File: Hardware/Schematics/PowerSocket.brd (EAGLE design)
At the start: 100 x 47.5 mm, 74 parts, among them T1 BT138-V, T2 BT138-V, T3 BT138-V, T4 BT138-V, T5 BT138-V, T6 BT138-V

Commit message: New board layout
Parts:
- removed ACIN-NULL, ACIN-PHASE, ACOUT-NULL, ACOUT-NULL1, ACOUT-NULL2, ACOUT-PHASE, ACOUT-PHASE1, ACOUT-PHASE2: -, wirepad:3,81/1,4
- removed BUTTON_LED+: BUTTON_VCC, wirepad:2,15/1,0
- removed BUTTON_LED+1, BUTTON_LED+2, BUTTON_LED-, BUTTON_LED-1, BUTTON_LED-2, BUTTON_SWITCH1, BUTTON_SWITCH3, BUTTON_SWITCH5: -, wirepad:2,15/1,0
- removed U$1, U$3, U$4: ACS710, PowerSocket:SO-16DW
- added AMP1, AMP2, AMP3: ACS710, PowerSocket:SO-16DW
- added BUTTON1_VCC: (no value), wirepad:2,15/1,0
- added BUTTON2_VCC, BUTTON3_VCC, LED1, LED2, LED3, SWITCH1, SWITCH2, SWITCH3: -, wirepad:2,15/1,0
- added NULL, NULL1-OUT, NULL2-OUT, NULL3-OUT, PHASE, PHASE1-OUT, PHASE2-OUT, PHASE3-OUT: -, wirepad:3,81/1,4
- added R24: 0, eagle-ltspice:R2010
- R14, R18: device rcl:C0805 -> rcl:R0805
- T1, T2, T3, T4, T5, T6: value BT138-V -> BT138-H; device triac:TO220BV -> triac:TO220BH
- moved R9 83.6 mm to (89.3, 19.7), turned to 270 degrees
- moved R10 79.9 mm to (80.9, 30.8), turned to 180 degrees
- moved C11 71.6 mm to (85.7, 27.1)
- moved R3 69.1 mm to (83.4, 26.1)
- moved C10 67.3 mm to (85.5, 20.0), flipped to the bottom
- moved R4 66.1 mm to (79.3, 19.3), turned to 0 degrees
- moved C9 65.5 mm to (81.1, 27.6), flipped to the bottom
- moved T2 56.8 mm to (61.0, 13.5), turned to 0 degrees
- moved R11 56.4 mm to (96.1, 56.7), flipped to the top
- moved R15 55.9 mm to (79.0, 29.2), turned to 180 degrees
- moved R12 55.7 mm to (89.3, 23.1), turned to 270 degrees
- moved OK2 55.3 mm to (61.0, 15.5)
- moved R13 52.5 mm to (77.1, 12.9), turned to 0 degrees
- moved C1 49.3 mm to (86.6, 31.4), flipped to the bottom
- moved C4 49.2 mm to (88.6, 31.4), flipped to the bottom
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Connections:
- net N$25 renamed GATE2
- net N$3 renamed VOLTMETER
- removed net N$15 (its old number): BUTTON_LED-.1, R7.1
- removed net N$2 (its old number): R1.1, RESET.4, U$2.EN
- removed net N$36 (its old number): ACOUT-PHASE1.1, U$3.5, U$3.6, U$3.7, U$3.8
- removed net N$40: U$3.13
- removed net N$42 (its old number): OK5.2, R16.2
- removed net N$43: OK5.6, R17.1
- removed net N$45: ACIN-NULL.1, R5.1, T1.T1, T3.T1, T5.T1
- removed net N$46: OK6.2, R18.1
- removed net N$47: OK6.6, R19.1
- removed net N$49: R19.2, T6.T2, U$4.1, U$4.2, U$4.3, U$4.4
- removed net N$50: U$4.13
- removed net N$51: ACIN-PHASE.1, D1.C, T2.T1, T4.T1, T6.T1
- removed net N$52: R22.2, U$2.IO5
- removed net N$53: R15.2, T4.T2, U$3.1, U$3.2, U$3.3, U$3.4
- removed net N$54: R16.1, R18.2, U$2.IO27
- removed net N$55: C9.2, U$1.11
- removed net N$60: C10.2, U$1.10
- removed net N$62: C1.2, U$3.11
- removed net N$63: C4.2, U$3.10
- removed net N$64: C5.2, U$4.11
- removed net N$65: C6.2, U$4.10
- new net AMP1: AMP1.12, U$2.IO34
- new net AMP2: AMP2.12, U$2.IO35
- new net AMP3: AMP3.12, U$2.IO32
- new net BUTTON1: R8.1, SWITCH1.1, U$2.IO22
- new net BUTTON2: R21.1, SWITCH2.1, U$2.IO23
- new net BUTTON3: R23.1, SWITCH3.1, U$2.IO5
- new net GATE1: R3.2, R9.2, U$2.IO25
- new net GATE3: R16.1, R18.1, U$2.IO27
- new net LED1: R7.2, U$2.IO19
- new net LED2: R20.2, U$2.IO18
- new net LED3: R22.2, U$2.IO17
- new net N$24: FLASH.3, FLASH.4, R2.2, U$2.IO0
- new net N$30: AMP2.10, C4.1
- new net N$66: R1.1, RESET.3, RESET.4, U$2.EN
- new net NULL: NULL.1, R5.1, T2.T1, T4.T1, T6.T1
- new net PHASE: PHASE.1, R24.2, T1.T1, T3.T1, T5.T1
- new net PHASE1: AMP1.1, AMP1.2, AMP1.3, AMP1.4, R10.2, T1.T2
- new net PHASE2: AMP2.1, AMP2.2, AMP2.3, AMP2.4, R15.2, T3.T2
- new net PHASE3: AMP3.1, AMP3.2, AMP3.3, AMP3.4, R19.2, T5.T2
- net GND: now also AMP1.16, AMP1.9, AMP2.16, AMP2.9, AMP3.16, AMP3.9, C1.2, C10.2, C11.2, C12.2, C13.2, C4.2, C5.2, C6.2, C9.2, FLASH.1, R21.2, R23.2, R8.2, RESET.2; no longer C1.1, C10.1, C11.1, C12.1, C13.1, C4.1, C5.1, C6.1, C9.1, R21.1, R23.1, R8.1, U$1.16, U$1.9, U$3.16, U$3.9, U$4.16, U$4.9
- net N$1: now also OK1.2, R9.1; no longer ACOUT-NULL.1, R4.2, T1.T2
- net N$10: now also AMP3.5, AMP3.6, AMP3.7, AMP3.8, PHASE3-OUT.1; no longer OK2.2, R9.1
- net N$11: now also LED3.1, R22.1; no longer U$2.IO35, U$3.12
- net N$12: now also AMP1.10, C10.1; no longer U$1.12, U$2.IO34
- net N$13: now also AMP1.11, C9.1; no longer ACOUT-PHASE.1, U$1.5, U$1.6, U$1.7, U$1.8
- net N$14: now also NULL2-OUT.1, T4.T2; no longer ACOUT-NULL1.1, T3.T2
- net N$16: now also OK4.6, R13.1; no longer BUTTON_LED-1.1, R20.1
- net N$17: now also NULL1-OUT.1, R4.2, T2.T2; no longer BUTTON_SWITCH1.1, R8.2, U$2.IO19
- net N$18: now also OK5.2, R18.2; no longer OK1.6, R4.1
- net N$20: now also OK1.6, R10.1; no longer BUTTON_SWITCH3.1, R21.2, U$2.IO18
- net N$21: now also R4.1; no longer R10.1
- net N$23: now also OK3.6, R15.1; no longer R10.2, T2.T2, U$1.1, U$1.2, U$1.3, U$1.4
- net N$26: now also AMP2.5, AMP2.6, AMP2.7, AMP2.8, PHASE2-OUT.1; no longer BUTTON_LED-2.1, R22.1
- net N$27: now also AMP1.5, AMP1.6, AMP1.7, AMP1.8, PHASE1-OUT.1; no longer U$1.13
- net N$28: now also R14.1; no longer R12.2
- net N$29: now also OK4.2, R12.2; no longer OK3.6, R13.1
- net N$31: now also OK6.2, R16.2; no longer R20.2, U$2.IO23
- net N$32: now also AMP2.11, C1.1; no longer OK4.2, R14.1
- net N$33: now also OK6.6, R17.1; no longer OK4.6, R15.1
- net N$35: now also OK5.6, R19.1; no longer ACOUT-PHASE2.1, U$4.5, U$4.6, U$4.7, U$4.8
- net N$38: now also AMP3.10, C6.1; no longer ACOUT-NULL2.1, R17.2, T5.T2
- net N$39: now also AMP3.11, C5.1; no longer BUTTON_SWITCH5.1, R23.2, U$2.IO17
- net N$41: now also D1.C, R24.1; no longer U$2.IO32, U$4.12
- net N$6: now also OK2.2, R3.1; no longer OK1.2, R3.2
- net N$7: now also LED2.1, R20.1; no longer FLASH.3, R2.2, U$2.IO0
- net N$8: now also NULL3-OUT.1, R17.2, T6.T2; no longer R3.1, R9.2, U$2.IO25
- net N$9: now also LED1.1, R7.1; no longer R7.2, U$2.IO22
- net VCC: now also AMP1.14, AMP1.15, AMP2.14, AMP2.15, AMP3.14, AMP3.15, BUTTON1_VCC.1, BUTTON2_VCC.1, BUTTON3_VCC.1, C11.1, C12.1, C13.1; no longer BUTTON_LED+.1, BUTTON_LED+1.1, BUTTON_LED+2.1, C11.2, C12.2, C13.2, U$1.14, U$1.15, U$3.14, U$3.15, U$4.14, U$4.15
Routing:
- net VCC: track 252.8 -> 0.00 mm, vias 10 -> 0
- net GND: track 181.0 -> 0.00 mm, vias 6 -> 0
- net N$8: track 93.5 -> 0.00 mm, vias 1 -> 0
- net N$12: track 87.8 -> 0.00 mm
- net N$11: track 70.5 -> 0.00 mm
- net N$45: track 59.3 -> 0.00 mm
- net N$51: track 58.8 -> 0.00 mm
- net GATE2: track 55.9 -> 0.00 mm, vias 2 -> 0
- net N$68: track 47.4 -> 0.00 mm
- net N$41: track 41.9 -> 0.00 mm, vias 2 -> 0
- net N$54: track 40.1 -> 0.00 mm, vias 1 -> 0
- net N$7: track 39.8 -> 0.00 mm, vias 3 -> 0
- net N$37: track 34.3 -> 0.00 mm
- net VOLTMETER: track 18.5 -> 0.00 mm, vias 1 -> 0
- net N$17: track 14.2 -> 0.00 mm, vias 1 -> 0
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- removed copper zone on layer 1, net GND
- removed copper zone on layer 16, net GND

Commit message: Added .brd script.
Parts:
- removed BUTTON1_VCC: (no value), wirepad:2,15/1,0
- removed BUTTON2_VCC, BUTTON3_VCC, LED1, LED2, LED3, SWITCH1, SWITCH2, SWITCH3: -, wirepad:2,15/1,0
- removed U$2: ESP3212LABELS, esp3212-ptw:ESP3212
- added BUTTON1, BUTTON2, BUTTON3: (no value), pinhead:1X03
- added ESP3212: ESP3212LABELS, esp3212-ptw:ESP3212
- moved C2 84.5 mm to (5.31, 73.5)
- moved R18 79.3 mm to (6.00, 24.0)
- moved C1 78.4 mm to (14.6, 62.2), flipped to the top, turned to 0 degrees
- moved R17 77.3 mm to (9.00, 10.0)
- moved R19 73.2 mm to (14.0, 41.0)
- moved C11 67.8 mm to (38.7, 75.9), flipped to the top
- moved R16 63.8 mm to (17.0, 23.5)
- moved C6 61.9 mm to (41.9, 67.6), flipped to the top, turned to 0 degrees
- moved C5 61.8 mm to (27.3, 65.8), flipped to the top, turned to 0 degrees
- moved SUPPLY_3.3 59.9 mm to (93.5, 1.96)
- moved C10 57.8 mm to (58.1, 71.0), flipped to the top, turned to 0 degrees
- moved SUPPLY_GND 57.2 mm to (93.5, 4.50)
- moved C4 54.3 mm to (49.4, 68.9), flipped to the top, turned to 0 degrees
- moved R12 50.3 mm to (39.0, 23.5)
- moved C9 49.1 mm to (40.4, 54.9), flipped to the top, turned to 0 degrees
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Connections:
- net AMP1: now also ESP3212.IO34; no longer U$2.IO34
- net AMP2: now also ESP3212.IO35; no longer U$2.IO35
- net AMP3: now also ESP3212.IO32; no longer U$2.IO32
- net BUTTON1: now also BUTTON1.3, ESP3212.IO22; no longer SWITCH1.1, U$2.IO22
- net BUTTON2: now also BUTTON2.3, ESP3212.IO23; no longer SWITCH2.1, U$2.IO23
- net BUTTON3: now also BUTTON3.3, ESP3212.IO5; no longer SWITCH3.1, U$2.IO5
- net GATE1: now also ESP3212.IO25; no longer U$2.IO25
- net GATE2: now also ESP3212.IO26; no longer U$2.IO26
- net GATE3: now also ESP3212.IO27; no longer U$2.IO27
- net GND: now also ESP3212.GND_B, ESP3212.GND_L, ESP3212.GND_R, ESP3212.IO2; no longer U$2.GND_B, U$2.GND_L, U$2.GND_R, U$2.IO2
- net LED1: now also ESP3212.IO19; no longer U$2.IO19
- net LED2: now also ESP3212.IO18; no longer U$2.IO18
- net LED3: now also ESP3212.IO17; no longer U$2.IO17
- net N$11: now also BUTTON3.2; no longer LED3.1
- net N$2: now also ESP3212.IO15; no longer U$2.IO15
- net N$24: now also ESP3212.IO0; no longer U$2.IO0
- net N$3: now also ESP3212.IO13; no longer U$2.IO13
- net N$4: now also ESP3212.IO12; no longer U$2.IO12
- net N$5: now also ESP3212.IO14; no longer U$2.IO14
- net N$66: now also ESP3212.EN; no longer U$2.EN
- net N$7: now also BUTTON2.2; no longer LED2.1
- net N$70: now also ESP3212.U0TX; no longer U$2.U0TX
- net N$77: now also ESP3212.U0RX; no longer U$2.U0RX
- net N$9: now also BUTTON1.2; no longer LED1.1
- net VCC: now also BUTTON1.1, BUTTON2.1, BUTTON3.1, ESP3212.3V3; no longer BUTTON1_VCC.1, BUTTON2_VCC.1, BUTTON3_VCC.1, U$2.3V3
- net VOLTMETER: now also ESP3212.IO4; no longer U$2.IO4
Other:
- board size 100 x 47.5 mm -> 100 x 80 mm

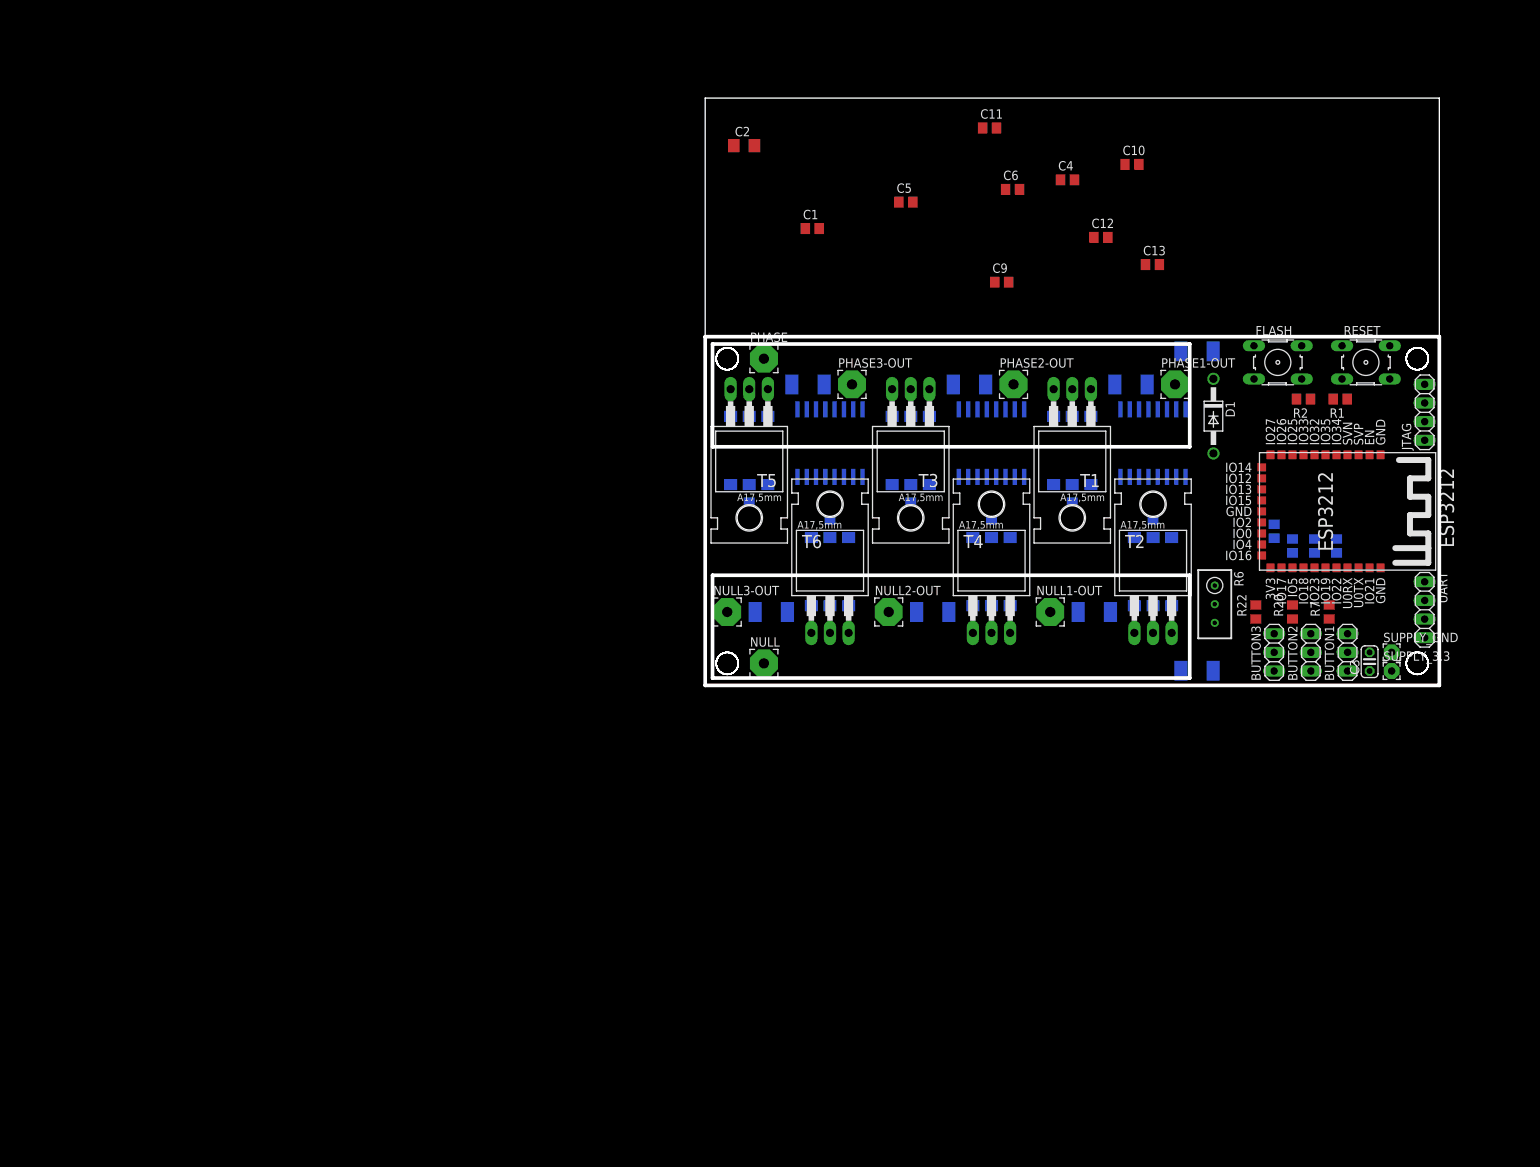
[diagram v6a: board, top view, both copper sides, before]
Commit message: Changed amp-meters and added 5V step-up. I probably don't have the correct package.
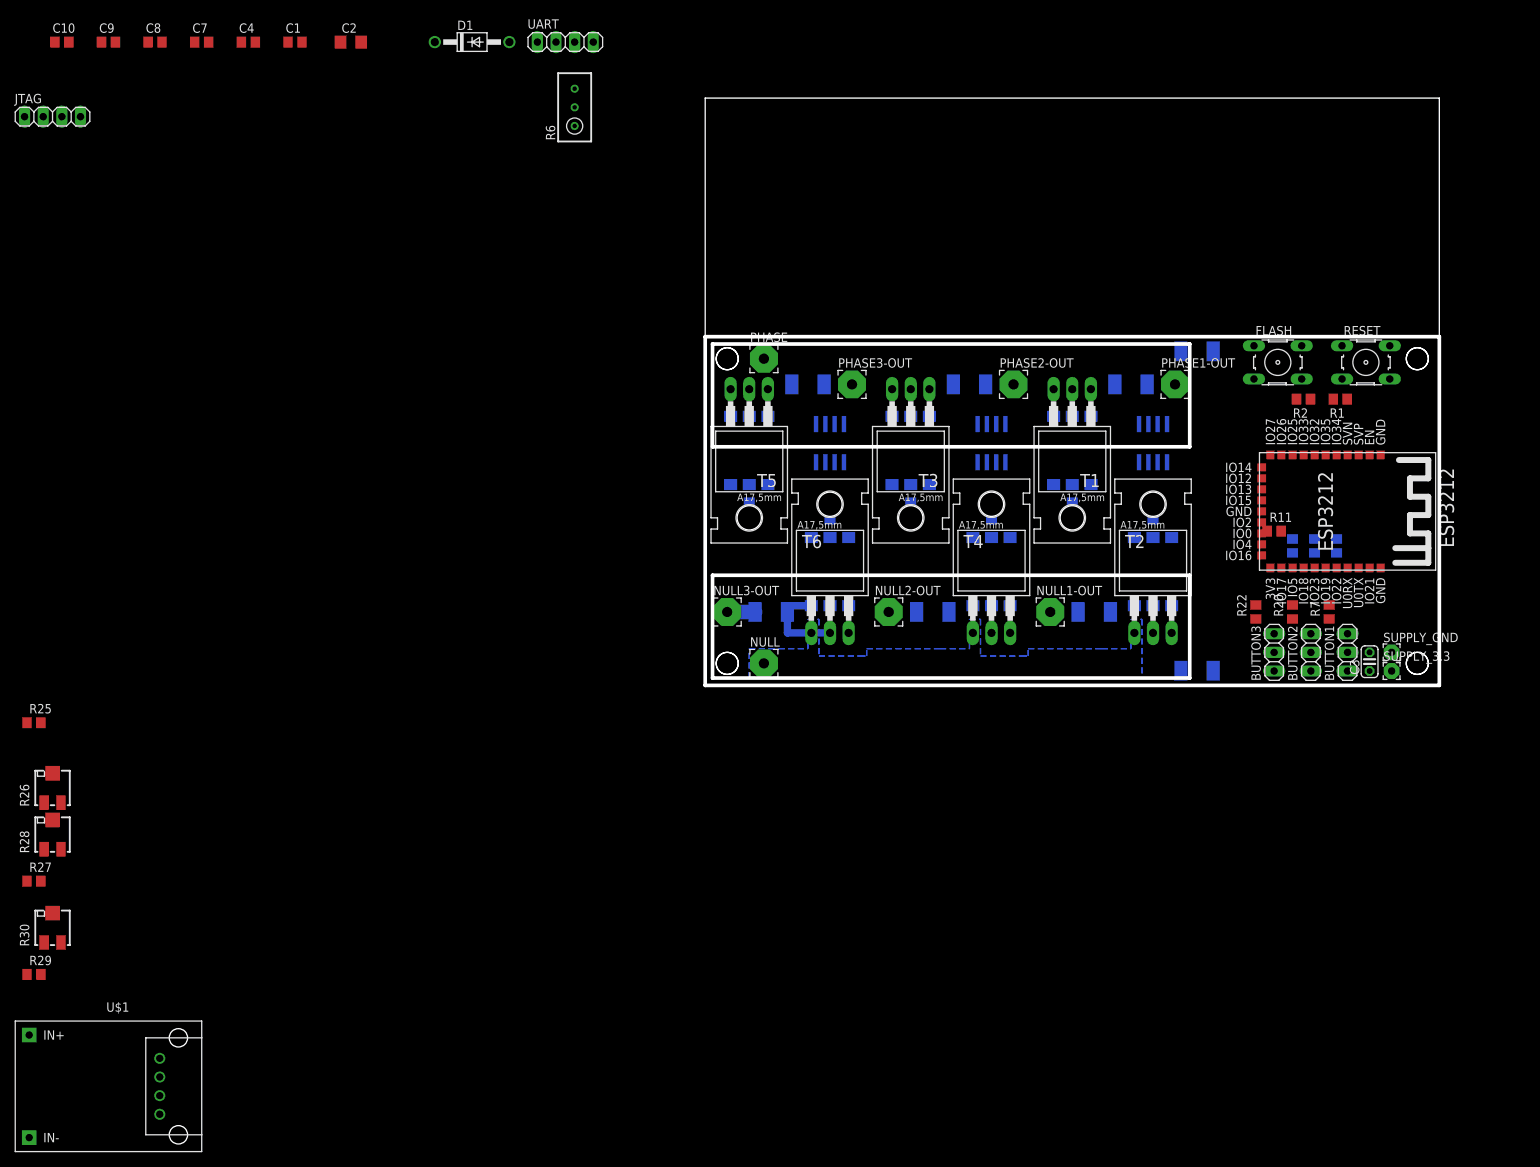
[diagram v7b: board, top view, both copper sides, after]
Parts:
- removed C11, C12, C13: 100nF, rcl:C0805
- removed C5: 470nF, rcl:C0805
- removed C6: 1nF, rcl:C0805
- added C7: 100nF, rcl:C0805
- added C8: 470nF, rcl:C0805
- added R25, R27, R29: 10K, rcl:R0805
- added R26, R28, R30: 10K, rcl:RTRIM5X
- added U$1: DC-DC-STEP-UP-5V, diy-modules:DC-DC-STEP-UP-5V
- AMP1, AMP2, AMP3: value ACS710 -> ACS712-LC; device PowerSocket:SO-16DW -> allegro-2:SOIC8
- C1, C9: value 470nF -> 100nF
- C10, C4: value 1nF -> 470nF
- moved JTAG 191.2 mm to (-88.9, 77.5), turned to 0 degrees
- moved C10 146.7 mm to (-87.6, 87.6)
- moved UART 140.3 mm to (-19.1, 87.6), turned to 0 degrees
- moved C9 126.0 mm to (-81.3, 87.6)
- moved C4 113.1 mm to (-62.2, 87.6)
- moved D1 113.1 mm to (-31.8, 87.6), turned to 0 degrees
- moved R6 110.4 mm to (-17.8, 78.7), turned to 0 degrees
- moved C1 74.9 mm to (-55.9, 87.6)
- moved C2 55.4 mm to (-48.3, 87.6)
- flipped R11 to the top, turned to 0 degrees
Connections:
- removed net N$30: AMP2.10, C4.1
- removed net N$32: AMP2.11, C1.1
- new net +5V: AMP1.8, AMP2.8, AMP3.8, C1.1, C7.1, C9.1, U$1.5V
- new net FLASH: ESP3212.IO25, FLASH.3, FLASH.4, R2.2
- new net N$37: AMP2.7, R25.2
- new net N$40: R29.1, R30.1
- new net N$43: AMP3.7, R29.2
- new net N$44: AMP1.7, R27.2
- net AMP1: now also R28.3; no longer AMP1.12
- net AMP2: now also R26.3; no longer AMP2.12
- net AMP3: now also R30.3; no longer AMP3.12
- net GATE1: now also ESP3212.IO0; no longer ESP3212.IO25
- net GATE2: now also ESP3212.IO4; no longer ESP3212.IO26
- net GATE3: now also ESP3212.IO16; no longer ESP3212.IO27
- net GND: now also AMP1.5, AMP2.5, AMP3.5, C7.2, C8.2, R26.2, R28.2, R30.2, U$1.D+, U$1.D-, U$1.GND, U$1.IN-; no longer AMP1.16, AMP1.9, AMP2.16, AMP2.9, AMP3.16, AMP3.9, C11.2, C12.2, C13.2, C5.2, C6.2
- net N$10: now also AMP3.3, AMP3.4; no longer AMP3.5, AMP3.6, AMP3.7, AMP3.8
- net N$12: now also AMP2.3, AMP2.4, PHASE2-OUT.1; no longer AMP1.10, C10.1
- net N$13: now also AMP2.6, C10.1; no longer AMP1.11, C9.1
- net N$24: now also AMP1.6, C8.1; no longer ESP3212.IO0, FLASH.3, FLASH.4, R2.2
- net N$26: now also AMP3.6, C4.1; no longer AMP2.5, AMP2.6, AMP2.7, AMP2.8, PHASE2-OUT.1
- net N$27: now also AMP1.3, AMP1.4; no longer AMP1.5, AMP1.6, AMP1.7, AMP1.8
- net N$38: now also R25.1, R26.1; no longer AMP3.10, C6.1
- net N$39: now also R27.1, R28.1; no longer AMP3.11, C5.1
- net PHASE1: no longer AMP1.3, AMP1.4
- net PHASE2: no longer AMP2.3, AMP2.4
- net PHASE3: no longer AMP3.3, AMP3.4
- net VCC: now also U$1.IN+; no longer AMP1.14, AMP1.15, AMP2.14, AMP2.15, AMP3.14, AMP3.15, C11.1, C12.1, C13.1
- net VOLTMETER: now also ESP3212.IO26; no longer ESP3212.IO4
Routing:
- net N$8: track 0.00 -> 12.4 mm
- net N$33: track 0.00 -> 4.12 mm
- added copper zone on layer 16, net N$30
- added copper zone on layer 16, net N$32
